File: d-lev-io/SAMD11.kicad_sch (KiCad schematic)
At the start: 28 parts, among them J6 PROG_HDR, SW1 SW_Push, SW2 SW_Push, SW3 SW_Push, U3 ATSAMD11D14A-M

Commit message: many board updates
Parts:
- added C8: .1u, Capacitor_SMD:C_0603_1608Metric, symbol Device:C_Small
- added C8: 10u, Capacitor_SMD:C_0603_1608Metric, symbol Device:C_Small
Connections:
- net +3V3: now also C8.2, C8.2
- net GND: now also C8.1, C8.1
- net USB.DM renamed USB.DN
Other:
- note added: "todo: decouple AREF with 1uF choose decoupling cap values here vs AP2112"
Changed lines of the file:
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@@
   (junction (at 177.8 88.9) (diameter 0) (color 0 0 0 0)
   )
+  (junction (at 86.36 118.11) (diameter 0) (color 0 0 0 0)
+  )
   (junction (at 261.62 85.725) (diameter 0) (color 0 0 0 0)
   )
@@
   )
   (junction (at 179.705 96.52) (diameter 0) (color 0 0 0 0)
+  )
+  (junction (at 86.614 106.299) (diameter 0) (color 0 0 0 0)
   )
   (junction (at 50.165 153.67) (diameter 0) (color 0 0 0 0)
@@
     (stroke (width 0) (type default))
   )
+  (wire (pts (xy 86.614 106.426) (xy 88.773 106.426))
+    (stroke (width 0) (type default))
+  )
   (wire (pts (xy 261.62 39.37) (xy 261.62 44.45))
     (stroke (width 0) (type default))
@@
     (stroke (width 0) (type default))
   )
+  (wire (pts (xy 83.82 106.299) (xy 86.614 106.299))
+    (stroke (width 0) (type default))
+  )
   (wire (pts (xy 274.32 125.095) (xy 274.32 123.19))
     (stroke (width 0) (type default))
   )
+  (wire (pts (xy 86.614 103.632) (xy 86.614 106.299))
+    (stroke (width 0) (type default))
+  )
   (wire (pts (xy 51.816 96.52) (xy 59.69 96.52))
     (stroke (width 0) (type default))
@@
     (stroke (width 0) (type default))
   )
+  (wire (pts (xy 86.614 106.299) (xy 86.614 106.426))
+    (stroke (width 0) (type default))
+  )
   (wire (pts (xy 152.4 104.14) (xy 166.37 104.14))
     (stroke (width 0) (type default))
@@
     (stroke (width 0) (type default))
   )
+  (wire (pts (xy 86.36 118.11) (xy 88.773 118.11))
+    (stroke (width 0) (type default))
+  )
+  (wire (pts (xy 83.82 109.601) (xy 83.82 106.299))
+    (stroke (width 0) (type default))
+  )
   (wire (pts (xy 246.38 85.725) (xy 247.65 85.725))
     (stroke (width 0) (type default))
@@
     (stroke (width 0) (type default))
   )
+  (wire (pts (xy 88.773 114.681) (xy 88.773 118.11))
+    (stroke (width 0) (type default))
+  )
   (wire (pts (xy 47.244 88.9) (xy 47.244 91.44))
     (stroke (width 0) (type default))
   )
+  (wire (pts (xy 83.82 118.11) (xy 83.82 114.681))
+    (stroke (width 0) (type default))
+  )
   (wire (pts (xy 261.62 44.45) (xy 261.62 47.625))
     (stroke (width 0) (type default))
@@
     (stroke (width 0) (type default))
   )
+  (wire (pts (xy 83.82 118.11) (xy 86.36 118.11))
+    (stroke (width 0) (type default))
+  )
   (wire (pts (xy 231.775 137.16) (xy 248.92 137.16))
     (stroke (width 0) (type default))
@@
     (stroke (width 0) (type default))
   )
+  (wire (pts (xy 86.36 119.38) (xy 86.36 118.11))
+    (stroke (width 0) (type default))
+  )
   (wire (pts (xy 147.32 93.98) (xy 142.24 93.98))
     (stroke (width 0) (type default))
@@
     (stroke (width 0) (type default))
   )
+  (wire (pts (xy 88.773 106.426) (xy 88.773 109.601))
+    (stroke (width 0) (type default))
+  )
   (wire (pts (xy 129.54 78.74) (xy 129.54 81.28))
     (stroke (width 0) (type default))
+  )
+  (text "todo: decouple AREF with 1uF\nchoose decoupling cap values here vs AP2112"
+    (at 180.34 61.595 0)
+    (effects (font (size 1.27 1.27)) (justify left bottom))
   )
   (text "https://blog.thea.codes/sam-d21-brown-out-detector/"
@@
     (effects (font (size 1.27 1.27)) (justify left bottom))
   )
-  (label "USB.DM" (at 166.37 121.92 180) (fields_autoplaced)
+  (label "USB.DN" (at 166.37 121.92 180) (fields_autoplaced)
     (effects (font (size 1.27 1.27)) (justify right bottom))
   )
@@
     (effects (font (size 1.27 1.27)) (justify left))
   )
-  (hierarchical_label "USB{DM,DP}" (shape bidirectional) (at 189.23 125.095 0) (fields_autoplaced)
+  (hierarchical_label "USB{DN,DP}" (shape bidirectional) (at 189.23 125.095 0) (fields_autoplaced)
     (effects (font (size 1.27 1.27)) (justify left))
   )
@@
     )
   )
+  (symbol (lib_id "Device:C_Small") (at 83.82 112.141 180) (unit 1)
+    (in_bom yes) (on_board yes) (dnp no) (fields_autoplaced)
+    (property "Reference" "C8" (at 86.36 111.4996 0)
+      (effects (font (size 1.27 1.27)) (justify right))
+    )
+    (property "Value" ".1u" (at 86.36 114.0396 0)
+      (effects (font (size 1.27 1.27)) (justify right))
+    )
+    (property "Footprint" "Capacitor_SMD:C_0603_1608Metric" (at 83.82 112.141 0)
+      (effects (font (size 1.27 1.27)) hide)
+    )
+    (property "Datasheet" "~" (at 83.82 112.141 0)
+      (effects (font (size 1.27 1.27)) hide)
+    )
+    (property "Tolerance" "" (at 83.82 112.141 0)
+      (effects (font (size 1.27 1.27)))
+    )
+    (pin "1")
+    (pin "2")
+    (instances
+      (project "d-lev-io"
+        (path "/9261a07b-ae4a-4d72-8042-ea097cd0e5ed"
+          (reference "C8") (unit 1)
+        )
+        (path "/9261a07b-ae4a-4d72-8042-ea097cd0e5ed/fd6a6c10-f456-4937-8c5d-f097bbb805c0"
+          (reference "C42") (unit 1)
+        )
+      )
+    )
+  )
   (symbol (lib_id "Device:R_Small") (at 261.62 123.19 270) (unit 1)
     (in_bom yes) (on_board yes) (dnp no)
@@
         (path "/9261a07b-ae4a-4d72-8042-ea097cd0e5ed/fd6a6c10-f456-4937-8c5d-f097bbb805c0"
           (reference "D3") (unit 1)
+        )
+      )
+    )
+  )
+  (symbol (lib_id "Device:C_Small") (at 88.773 112.141 180) (unit 1)
+    (in_bom yes) (on_board yes) (dnp no) (fields_autoplaced)
+    (property "Reference" "C8" (at 91.821 111.4996 0)
+      (effects (font (size 1.27 1.27)) (justify right))
+    )
+    (property "Value" "10u" (at 91.821 114.0396 0)
+      (effects (font (size 1.27 1.27)) (justify right))
+    )
+    (property "Footprint" "Capacitor_SMD:C_0603_1608Metric" (at 88.773 112.141 0)
+      (effects (font (size 1.27 1.27)) hide)
+    )
+    (property "Datasheet" "~" (at 88.773 112.141 0)
+      (effects (font (size 1.27 1.27)) hide)
+    )
+    (pin "1")
+    (pin "2")
+    (instances
+      (project "d-lev-io"
+        (path "/9261a07b-ae4a-4d72-8042-ea097cd0e5ed"
+          (reference "C8") (unit 1)
+        )
+        (path "/9261a07b-ae4a-4d72-8042-ea097cd0e5ed/fd6a6c10-f456-4937-8c5d-f097bbb805c0"
+          (reference "C41") (unit 1)
         )
       )
@@
     )
   )
+  (symbol (lib_id "power:GND") (at 86.36 119.38 0) (unit 1)
+    (in_bom yes) (on_board yes) (dnp no) (fields_autoplaced)
+    (property "Reference" "#PWR012" (at 86.36 125.73 0)
+      (effects (font (size 1.27 1.27)) hide)
+    )
+    (property "Value" "GND" (at 88.265 120.6499 0)
+      (effects (font (size 1.27 1.27)) (justify left))
+    )
+    (property "Footprint" "" (at 86.36 119.38 0)
+      (effects (font (size 1.27 1.27)) hide)
+    )
+    (property "Datasheet" "" (at 86.36 119.38 0)
+      (effects (font (size 1.27 1.27)) hide)
+    )
+    (pin "1")
+    (instances
+      (project "d-lev-io"
+        (path "/9261a07b-ae4a-4d72-8042-ea097cd0e5ed"
+          (reference "#PWR012") (unit 1)
+        )
+        (path "/9261a07b-ae4a-4d72-8042-ea097cd0e5ed/fd6a6c10-f456-4937-8c5d-f097bbb805c0"
+          (reference "#PWR073") (unit 1)
+        )
+      )
+      (project "dlev-mini"
+        (path "/eb5e8bfd-9871-4528-bf57-58851bf63907/6062d07e-a4ed-44ac-a6b0-014aac464169"
+          (reference "#PWR0139") (unit 1)
+        )
+      )
+    )
+  )
   (symbol (lib_id "Connector:TestPoint") (at 179.705 96.52 0) (unit 1)
     (in_bom yes) (on_board yes) (dnp no) (fields_autoplaced)
@@
         )
       )
+    )
+  )
+  (symbol (lib_id "power:+3V3") (at 86.614 103.632 0) (unit 1)
+    (in_bom yes) (on_board yes) (dnp no)
+    (property "Reference" "#PWR018" (at 86.614 107.442 0)
+      (effects (font (size 1.27 1.27)) hide)
+    )
+    (property "Value" "+3V3" (at 86.614 98.552 0)
+      (effects (font (size 1.27 1.27)))
+    )
+    (property "Footprint" "" (at 86.614 103.632 0)
+      (effects (font (size 1.27 1.27)) hide)
+    )
+    (property "Datasheet" "" (at 86.614 103.632 0)
+      (effects (font (size 1.27 1.27)) hide)
+    )
+    (pin "1")
+    (instances
+      (project "d-lev-io"
+        (path "/9261a07b-ae4a-4d72-8042-ea097cd0e5ed"
+          (reference "#PWR018") (unit 1)
+        )
+        (path "/9261a07b-ae4a-4d72-8042-ea097cd0e5ed/fd6a6c10-f456-4937-8c5d-f097bbb805c0"
+          (reference "#PWR072") (unit 1)
+        )
+      )

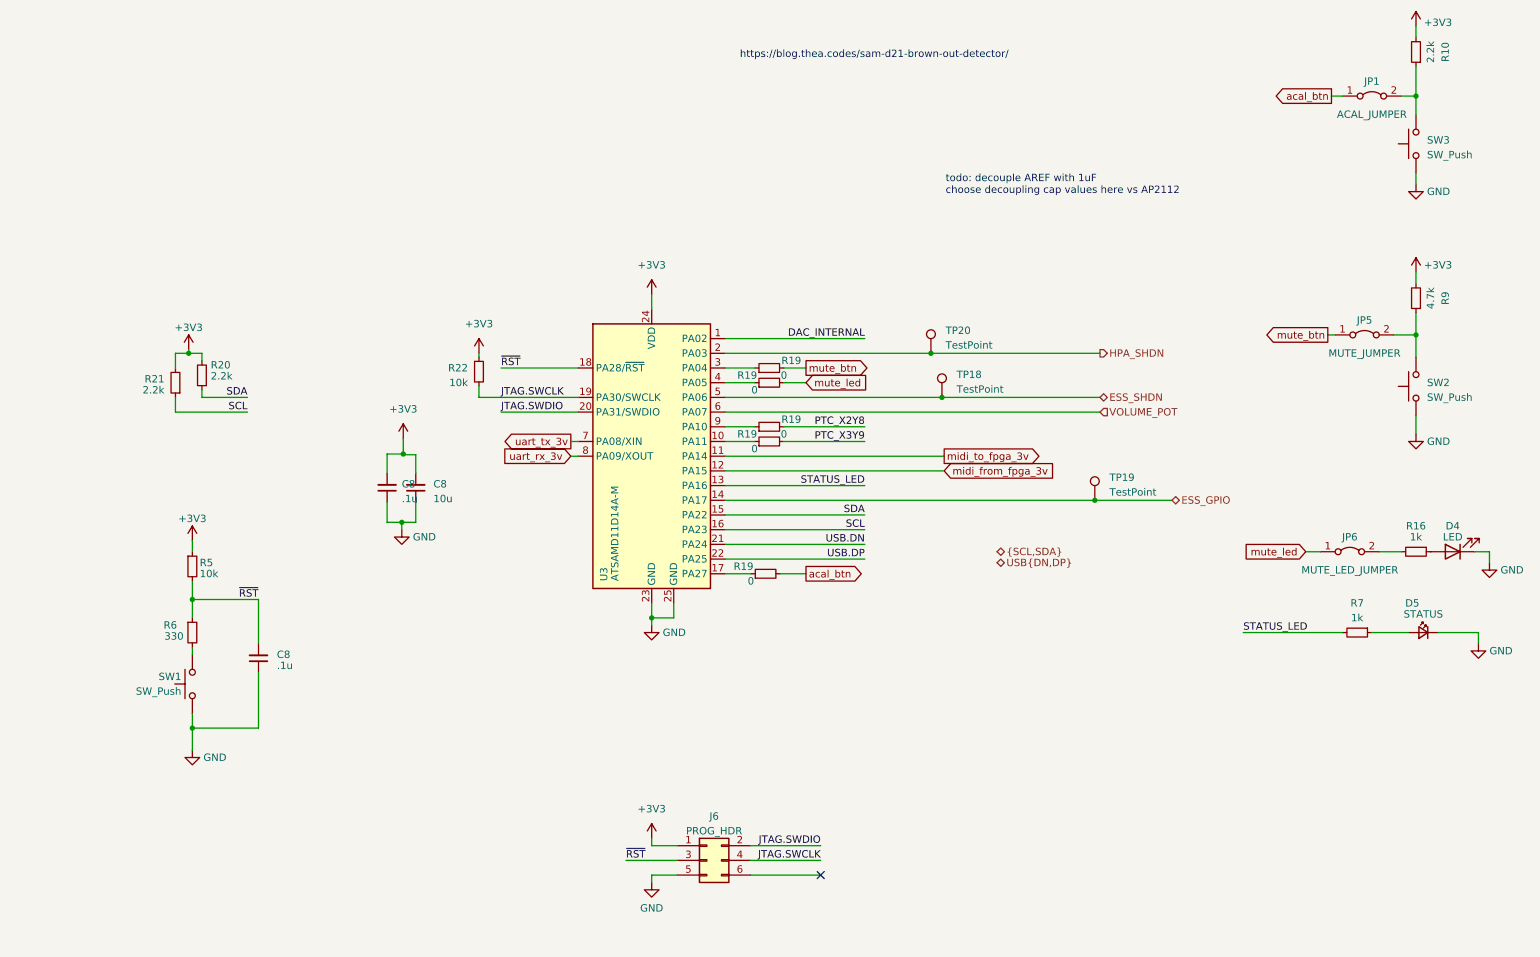
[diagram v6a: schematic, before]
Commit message: Routed IO board
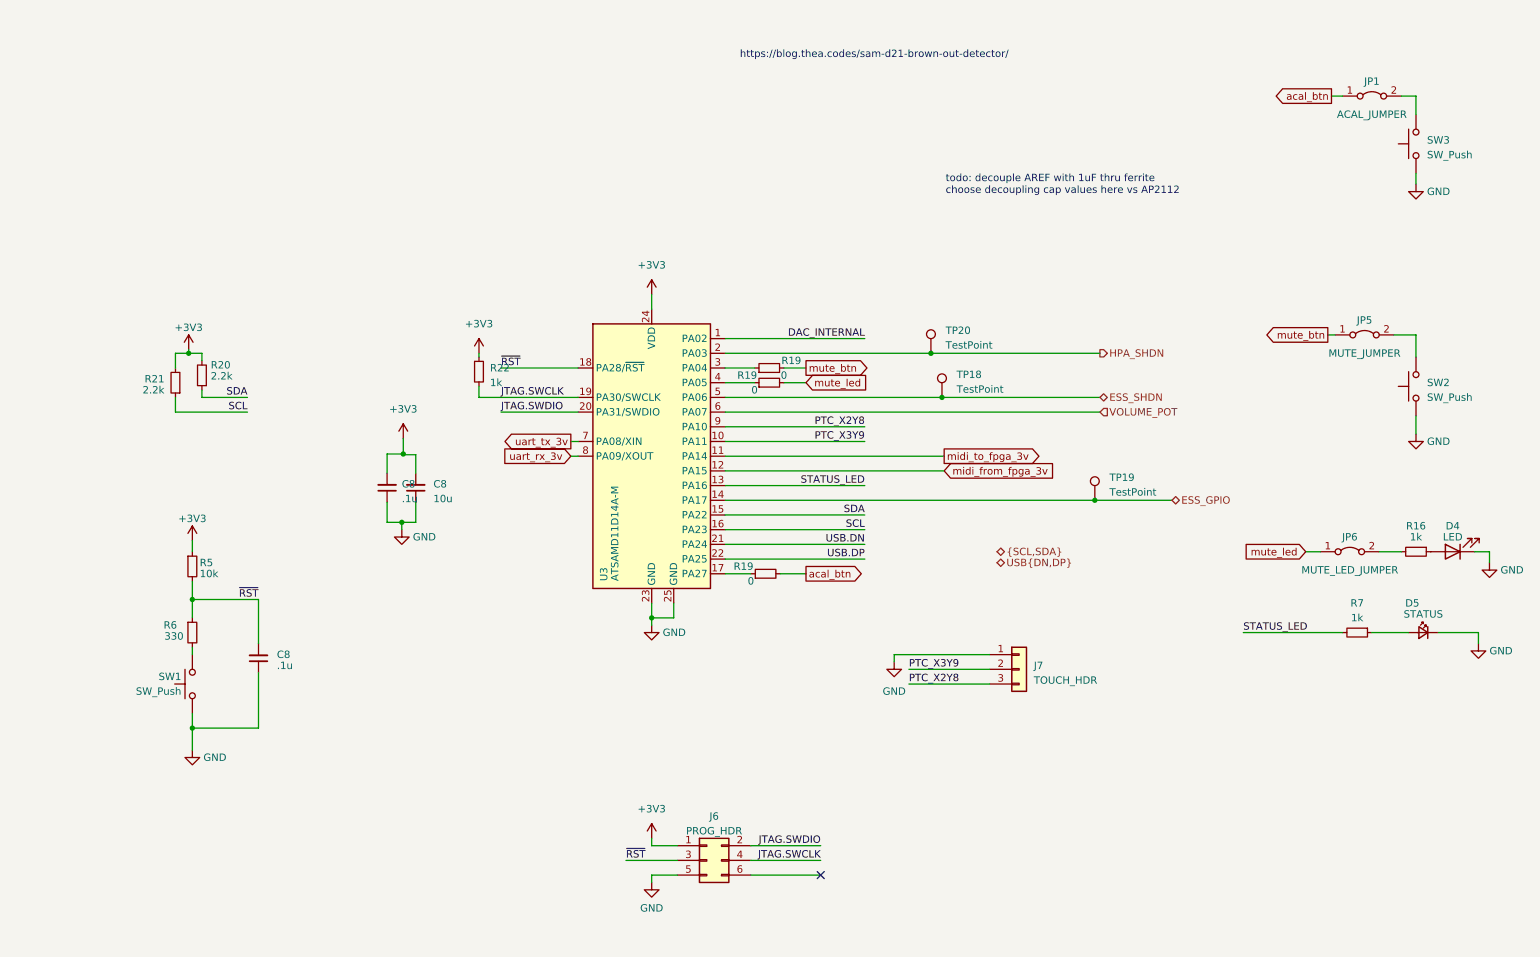
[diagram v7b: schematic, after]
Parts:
- removed R10: 2.2k, Resistor_SMD:R_0603_1608Metric, symbol Device:R_Small
- removed R19 (x2): 0, Resistor_SMD:R_0603_1608Metric, symbol Device:R_Small
- removed R9: 4.7k, Resistor_SMD:R_0603_1608Metric, symbol Device:R_Small
- added J7: TOUCH_HDR, Connector_PinHeader_2.54mm:PinHeader_1x03_P2.54mm_Vertical, symbol Connector_Generic:Conn_01x03
- R22: value 10k -> 1k
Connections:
- net GND: now also J7.1 (Pin_1)
- net PTC_X2Y8: now also U3.9 (PA10), J7.3 (Pin_3)
- net PTC_X3Y9: now also U3.10 (PA11), J7.2 (Pin_2)
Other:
- note added: "todo: decouple AREF with 1uF thru ferrite choose decoupling cap values here vs AP2112"
- note removed: "todo: decouple AREF with 1uF choose decoupling cap values here vs AP2112"

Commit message: add 5-pin CV expansion header
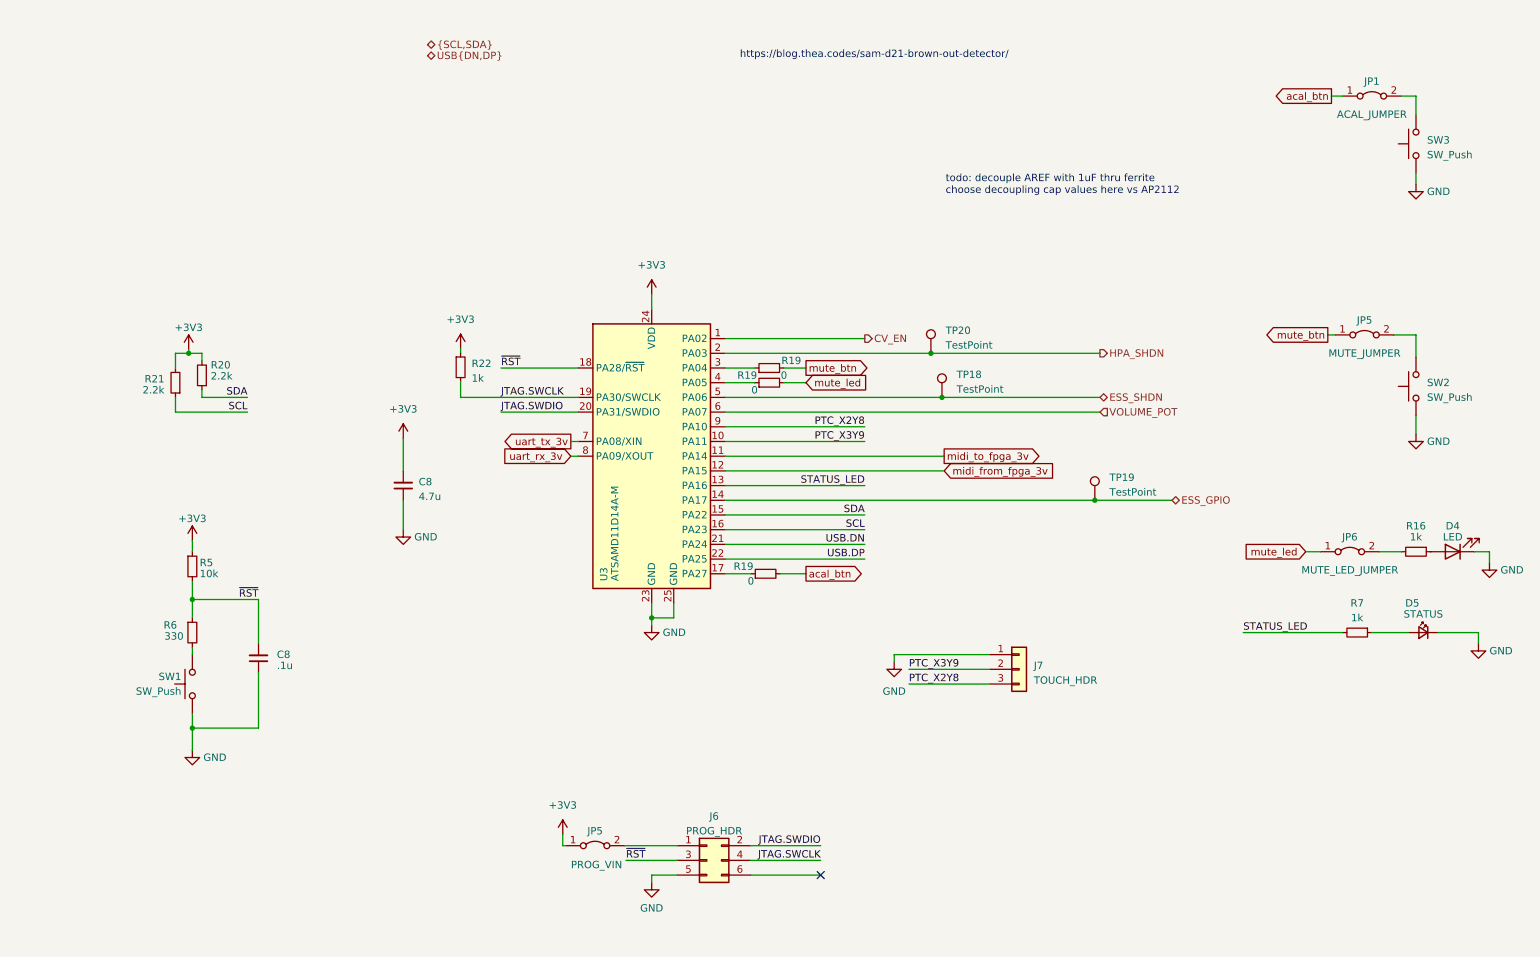
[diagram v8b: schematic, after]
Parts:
- removed C8: .1u, Capacitor_SMD:C_0603_1608Metric, symbol Device:C_Small
- added JP5: PROG_VIN, theremin:SolderJumper-2_P1.3mm_Open_TrianglePad1.0x1.5mm, symbol Jumper:Jumper_2_Bridged
- C8: value 10u -> 4.7u
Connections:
- net +3V3: now also JP5.1 (A); no longer J6.1 (Pin_1)
- net DAC_INTERNAL renamed CV_EN
- new net: J6.1 (Pin_1), JP5.2 (B)
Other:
- moved on the sheet: C8, R22
